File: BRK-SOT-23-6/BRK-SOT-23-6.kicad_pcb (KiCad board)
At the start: 2 copper layers, 18.3 x 18 mm, 3 parts, among them J1 Conn_01x03, J2 Conn_01x03, U1 SC-70-6

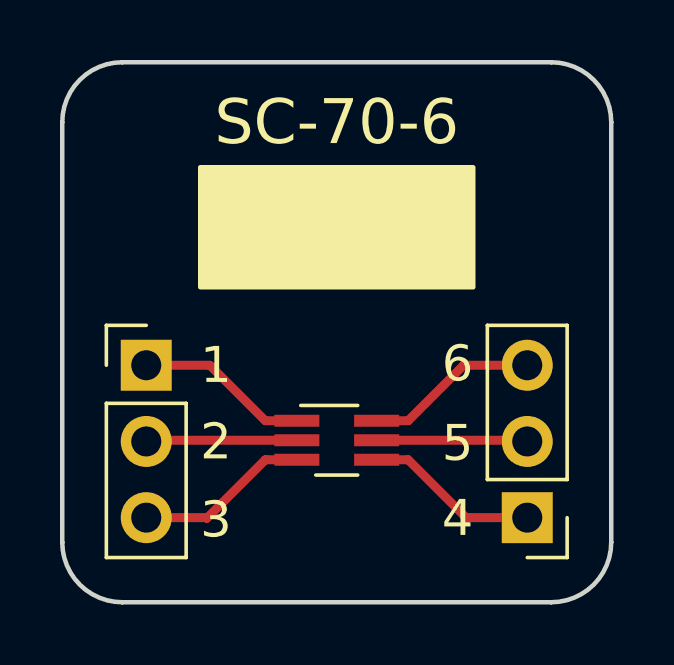
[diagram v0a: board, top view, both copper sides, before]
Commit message: BRK-SOT-23-6, BSK-MSOP-8-3x3-P0.65, BRK-VSSOP-8-2.4x2.1-P0.5
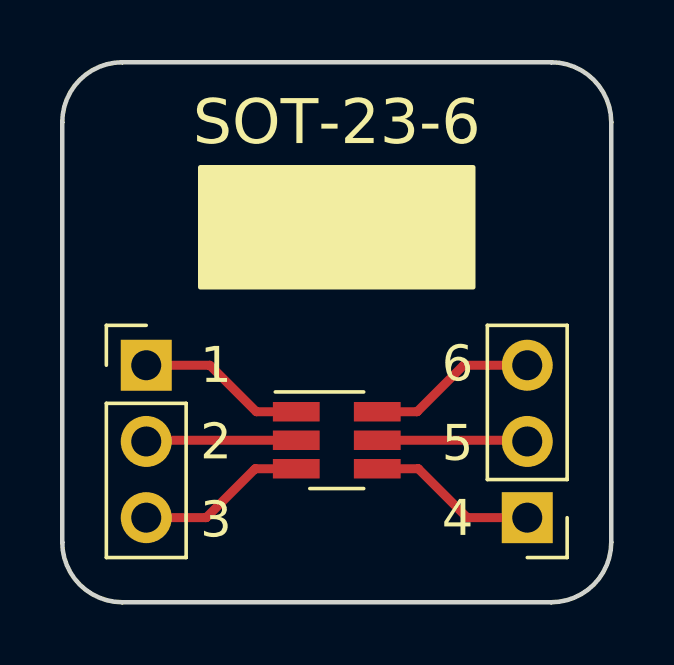
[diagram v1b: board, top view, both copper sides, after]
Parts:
- U1: value SC-70-6 -> SOT-23-6; footprint Package_TO_SOT_SMD:SOT-363_SC-70-6_Handsoldering -> Package_TO_SOT_SMD:SOT-23-6_Handsoldering
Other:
- board text added: "SOT-23-6"
- board text removed: "SC-70-6"

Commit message: Update several breakout boards
* Reduce distance from edge to pin header
* Enlarge silk screen area
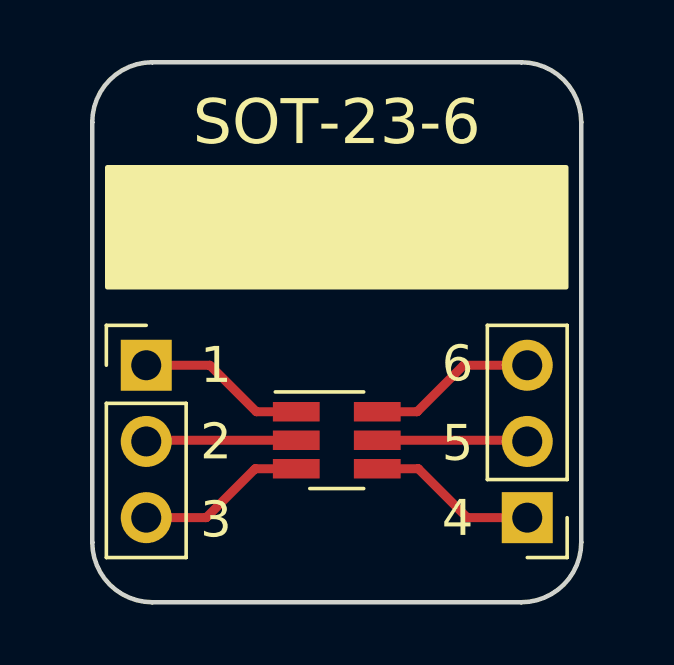
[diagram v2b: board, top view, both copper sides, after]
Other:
- board size 18.3 x 18 mm -> 16.3 x 18 mm
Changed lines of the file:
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@@
-(kicad_pcb (version 20171130) (host pcbnew 5.0.1-33cea8e~68~ubuntu18.10.1)
+(kicad_pcb (version 20171130) (host pcbnew 5.1.4-e60b266~84~ubuntu19.04.1)
   (general
-    (thickness 1.6)
+    (thickness 1)
     (drawings 16)
     (tracks 16)
@@
   (title_block
     (title BRK-SOT-23-6)
-    (rev v1.0)
+    (rev v1.1)
     (company https://gekkio.fi)
   )
@@
     (zone_45_only no)
     (trace_min 0.2)
-    (segment_width 0.2)
-    (edge_width 0.15)
     (via_size 0.8)
     (via_drill 0.4)
@@
     (uvia_min_size 0.2)
     (uvia_min_drill 0.1)
+    (edge_width 0.15)
+    (segment_width 0.2)
     (pcb_text_width 0.3)
     (pcb_text_size 1.5 1.5)
@@
     )
   )
-  (gr_arc (start 52 66) (end 50 66) (angle -90) (layer Edge.Cuts) (width 0.15))
-  (gr_arc (start 66.3 66) (end 66.3 68) (angle -90) (layer Edge.Cuts) (width 0.15))
-  (gr_arc (start 66.3 52) (end 68.3 52) (angle -90) (layer Edge.Cuts) (width 0.15))
-  (gr_arc (start 52 52) (end 52 50) (angle -90) (layer Edge.Cuts) (width 0.15))
+  (gr_arc (start 53 66) (end 51 66) (angle -90) (layer Edge.Cuts) (width 0.15))
+  (gr_arc (start 65.3 66) (end 65.3 68) (angle -90) (layer Edge.Cuts) (width 0.15))
+  (gr_arc (start 65.3 52) (end 67.3 52) (angle -90) (layer Edge.Cuts) (width 0.15))
+  (gr_arc (start 53 52) (end 53 50) (angle -90) (layer Edge.Cuts) (width 0.15))
   (gr_text 4 (at 63.7 65.2) (layer F.SilkS)
     (effects (font (size 1.2 1.2) (thickness 0.3)) (justify right))
@@
     (effects (font (size 1.2 1.2) (thickness 0.3)) (justify left))
   )
-  (gr_line (start 66.3 68) (end 52 68) (layer Edge.Cuts) (width 0.15))
-  (gr_poly (pts (xy 54.6 53.5) (xy 54.6 57.5) (xy 63.7 57.5) (xy 63.7 53.5)) (layer F.SilkS) (width 0.15))
-  (gr_line (start 68.3 52) (end 68.3 66) (layer Edge.Cuts) (width 0.15))
+  (gr_line (start 65.3 68) (end 53 68) (layer Edge.Cuts) (width 0.15))
+  (gr_poly (pts (xy 51.5 53.5) (xy 51.5 57.5) (xy 66.8 57.5) (xy 66.8 53.5)) (layer F.SilkS) (width 0.15))
+  (gr_line (start 67.3 52) (end 67.3 66) (layer Edge.Cuts) (width 0.15))
   (gr_text SOT-23-6 (at 59.15 52) (layer F.SilkS)
     (effects (font (size 1.5 1.5) (thickness 0.3)))
   )
-  (gr_line (start 52 50) (end 66.3 50) (layer Edge.Cuts) (width 0.15))
-  (gr_line (start 50 66) (end 50 52) (layer Edge.Cuts) (width 0.15))
+  (gr_line (start 53 50) (end 65.3 50) (layer Edge.Cuts) (width 0.15))
+  (gr_line (start 51 66) (end 51 52) (layer Edge.Cuts) (width 0.15))
   (segment (start 54.92 60.1) (end 52.8 60.1) (width 0.3) (layer F.Cu) (net 1) (status 20))
   (segment (start 56.47 61.65) (end 57.8 61.65) (width 0.3) (layer F.Cu) (net 1) (status 20))
